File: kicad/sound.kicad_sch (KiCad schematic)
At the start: 17 parts, among them J4 Speaker, U11 74HC02, U16 74HC00, U17 LM386, U3 PSG_AY-3-8912

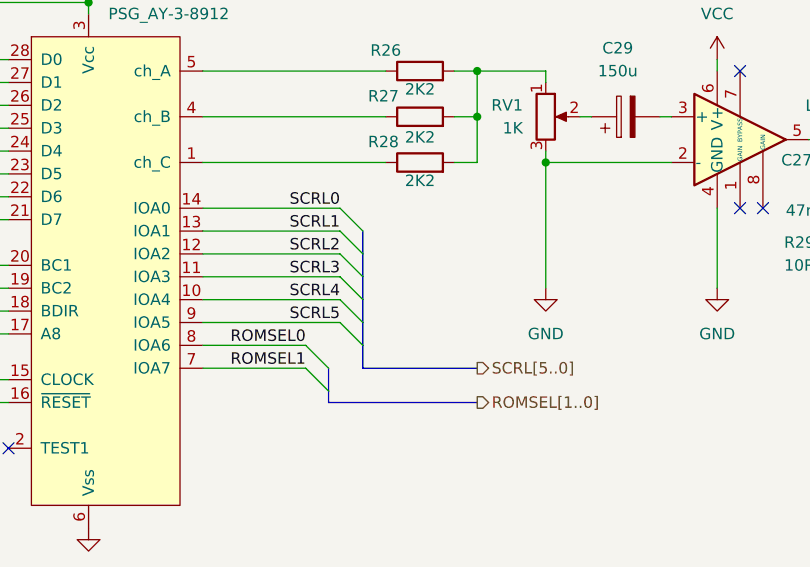
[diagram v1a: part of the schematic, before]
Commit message: hw: color text mode VGA (WIP)
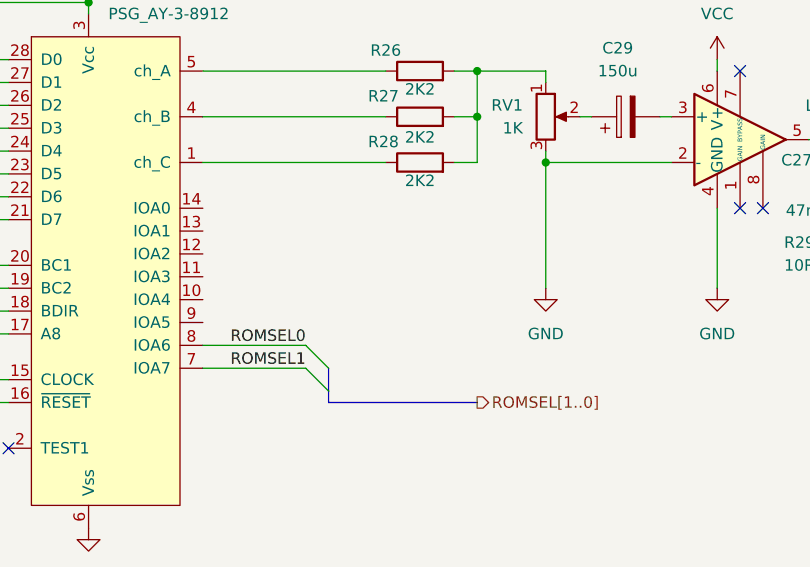
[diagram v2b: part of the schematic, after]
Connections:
- net SCRL0: no longer names the net of U3.14 (IOA0)
- net SCRL1: no longer names the net of U3.13 (IOA1)
- net SCRL2: no longer names the net of U3.12 (IOA2)
- net SCRL3: no longer names the net of U3.11 (IOA3)
- net SCRL4: no longer names the net of U3.10 (IOA4)
- net SCRL5: no longer names the net of U3.9 (IOA5)
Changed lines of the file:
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@@
-	)
-	(bus_entry
-		(at 161.29 93.98)
-		(size -2.54 -2.54)
-		(stroke
-			(width 0)
-			(type default)
-		)
 	)
 	(bus_entry
@@
 	)
 	(bus_entry
-		(at 161.29 101.6)
-		(size -2.54 -2.54)
-		(stroke
-			(width 0)
-			(type default)
-		)
-	)
-	(bus_entry
 		(at 109.22 74.93)
 		(size 2.54 2.54)
@@
 	)
 	(bus_entry
-		(at 161.29 96.52)
-		(size -2.54 -2.54)
-		(stroke
-			(width 0)
-			(type default)
-		)
-	)
-	(bus_entry
-		(at 161.29 106.68)
-		(size -2.54 -2.54)
-		(stroke
-			(width 0)
-			(type default)
-		)
-	)
-	(bus_entry
-		(at 161.29 104.14)
-		(size -2.54 -2.54)
-		(stroke
-			(width 0)
-			(type default)
-		)
-	)
-	(bus_entry
-		(at 161.29 99.06)
-		(size -2.54 -2.54)
-		(stroke
-			(width 0)
-			(type default)
-		)
-	)
-	(bus_entry
 		(at 109.22 87.63)
 		(size 2.54 2.54)
@@
 		)
 	)
-	(wire
-		(pts
-			(xy 143.51 91.44) (xy 158.75 91.44)
-		)
-		(stroke
-			(width 0)
-			(type default)
-		)
-	)
 	(bus
 		(pts
@@
 		)
 	)
-	(bus
-		(pts
-			(xy 161.29 106.68) (xy 161.29 109.22)
-		)
-		(stroke
-			(width 0)
-			(type default)
-		)
-	)
 	(wire
 		(pts
@@
 		)
 	)
-	(wire
-		(pts
-			(xy 143.51 99.06) (xy 158.75 99.06)
-		)
-		(stroke
-			(width 0)
-			(type default)
-		)
-	)
 	(bus
 		(pts
@@
 		)
 	)
-	(bus
-		(pts
-			(xy 161.29 99.06) (xy 161.29 101.6)
-		)
-		(stroke
-			(width 0)
-			(type default)
-		)
-	)
 	(wire
 		(pts
@@
 	(wire
 		(pts
-			(xy 143.51 93.98) (xy 158.75 93.98)
-		)
-		(stroke
-			(width 0)
-			(type default)
-		)
-	)
-	(wire
-		(pts
 			(xy 143.51 106.68) (xy 154.94 106.68)
 		)
@@
 	(bus
 		(pts
-			(xy 161.29 109.22) (xy 173.99 109.22)
-		)
-		(stroke
-			(width 0)
-			(type default)
-		)
-	)
-	(bus
-		(pts
 			(xy 157.48 109.22) (xy 157.48 111.76)
 		)
@@
 	(wire
 		(pts
-			(xy 143.51 104.14) (xy 158.75 104.14)
-		)
-		(stroke
-			(width 0)
-			(type default)
-		)
-	)
-	(wire
-		(pts
 			(xy 173.99 76.2) (xy 181.61 76.2)
 		)
@@
 		)
 	)
-	(bus
-		(pts
-			(xy 161.29 96.52) (xy 161.29 99.06)
-		)
-		(stroke
-			(width 0)
-			(type default)
-		)
-	)
-	(wire
-		(pts
-			(xy 143.51 96.52) (xy 158.75 96.52)
-		)
-		(stroke
-			(width 0)
-			(type default)
-		)
-	)
 	(wire
 		(pts
@@
 		)
 	)
-	(bus
-		(pts
-			(xy 161.29 93.98) (xy 161.29 96.52)
-		)
-		(stroke
-			(width 0)
-			(type default)
-		)
-	)
 	(wire
 		(pts
@@
 	(wire
 		(pts
-			(xy 143.51 101.6) (xy 158.75 101.6)
-		)
-		(stroke
-			(width 0)
-			(type default)
-		)
-	)
-	(wire
-		(pts
 			(xy 185.42 81.28) (xy 186.69 81.28)
 		)
@@
 		)
 	)
-	(bus
-		(pts
-			(xy 161.29 104.14) (xy 161.29 106.68)
-		)
-		(stroke
-			(width 0)
-			(type default)
-		)
-	)
 	(wire
 		(pts
@@
 		)
 	)
-	(bus
-		(pts
-			(xy 161.29 101.6) (xy 161.29 104.14)
-		)
-		(stroke
-			(width 0)
-			(type default)
-		)
-	)
 	(wire
 		(pts
@@
 			(width 0)
 			(type default)
-		)
-	)
-	(label "SCRL3"
-		(at 158.75 99.06 180)
-		(effects
-			(font
-				(size 1.27 1.27)
-			)
-			(justify right bottom)
-		)
-	)
-	(label "SCRL2"
-		(at 158.75 96.52 180)
-		(effects
-			(font
-				(size 1.27 1.27)
-			)
-			(justify right bottom)
 		)
 	)
@@
 		)
 	)
-	(label "SCRL0"
-		(at 158.75 91.44 180)
-		(effects
-			(font
-				(size 1.27 1.27)
-			)
-			(justify right bottom)
-		)
-	)
-	(label "SCRL5"
-		(at 158.75 104.14 180)
-		(effects
-			(font
-				(size 1.27 1.27)
-			)
-			(justify right bottom)
-		)
-	)
 	(label "ROMSEL1"
 		(at 154.94 109.22 180)
@@
 		)
 	)
-	(label "SCRL1"
-		(at 158.75 93.98 180)
-		(effects
-			(font
-				(size 1.27 1.27)
-			)
-			(justify right bottom)
-		)
-	)
 	(label "D5"
 		(at 111.76 87.63 0)
@@
 			)
 			(justify left bottom)
-		)
-	)
-	(label "SCRL4"
-		(at 158.75 101.6 180)
-		(effects
-			(font
-				(size 1.27 1.27)
-			)
-			(justify right bottom)
 		)
 	)
@@
 		)
 	)
-	(hierarchical_label "SCRL[5..0]"
-		(shape output)
-		(at 173.99 109.22 0)
-		(effects
-			(font
-				(size 1.27 1.27)
-			)
-			(justify left)
-		)
-	)

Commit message: hw: finish schematic, start routing
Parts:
- removed U11: 74HC02, Package_DIP:DIP-14_W7.62mm, symbol 74xx:74HC02
- removed U16: 74HC00, Package_DIP:DIP-14_W7.62mm, symbol 74xx:74HC00
- added U33: GAL16V8, Package_DIP:DIP-20_W7.62mm, symbol Logic_Programmable:GAL16V8
- J4: footprint Connector_PinHeader_2.54mm:PinHeader_1x02_P2.54mm_Horizontal -> Connector_PinHeader_2.54mm:PinHeader_1x02_P2.54mm_Vertical
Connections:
- net A0: now also U33.2 (I2)
- net CLK: now also U33.1 (I1/CLK); no longer U3.15 (CLOCK)
- net GND: now also U33.10 (GND), U33.11 (I10/~{OE}), U33.6 (I6), U33.7 (I7), U33.8 (I8)
- net VCC: now also U33.20 (VCC)
- net ~{CS}: now also U33.3 (I3)
- net ~{RD}: now also U33.4 (I4)
- net ~{WR}: now also U33.5 (I5)
- net at U3.18 (BDIR): now also U33.15 (IO5)
- net SCROLL4: now reaches U3.10 (IOA4)
- net SCROLL3: now reaches U3.11 (IOA3)
- net SCROLL2: now reaches U3.12 (IOA2)
- net SCROLL1: now reaches U3.13 (IOA1)
- net SCROLL0: now reaches U3.14 (IOA0)
- net at U3.20 (BC1): now also U33.16 (IO4)
- net SCROLL5: now reaches U3.9 (IOA5)
- new net: U3.15 (CLOCK), U33.13 (IO7)
- new net A: U33.9 (I9)
- new net ~{A}: U33.12 (IO8)
- no-connect marks 4 -> 8
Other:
- company: (none) -> A.K.
- title: (none) -> Sound

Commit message: hw: finish routing
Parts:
- U3: value PSG_AY-3-8912 -> AY-3-8912
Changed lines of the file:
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@@
 			)
 		)
-		(property "Value" "PSG_AY-3-8912"
+		(property "Value" "AY-3-8912"
 			(at 133.0041 69.85 0)
 			(effects
